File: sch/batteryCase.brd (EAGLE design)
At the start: 68.2 x 27.9 mm, 7 parts, among them X1 C-GRID-04-70553

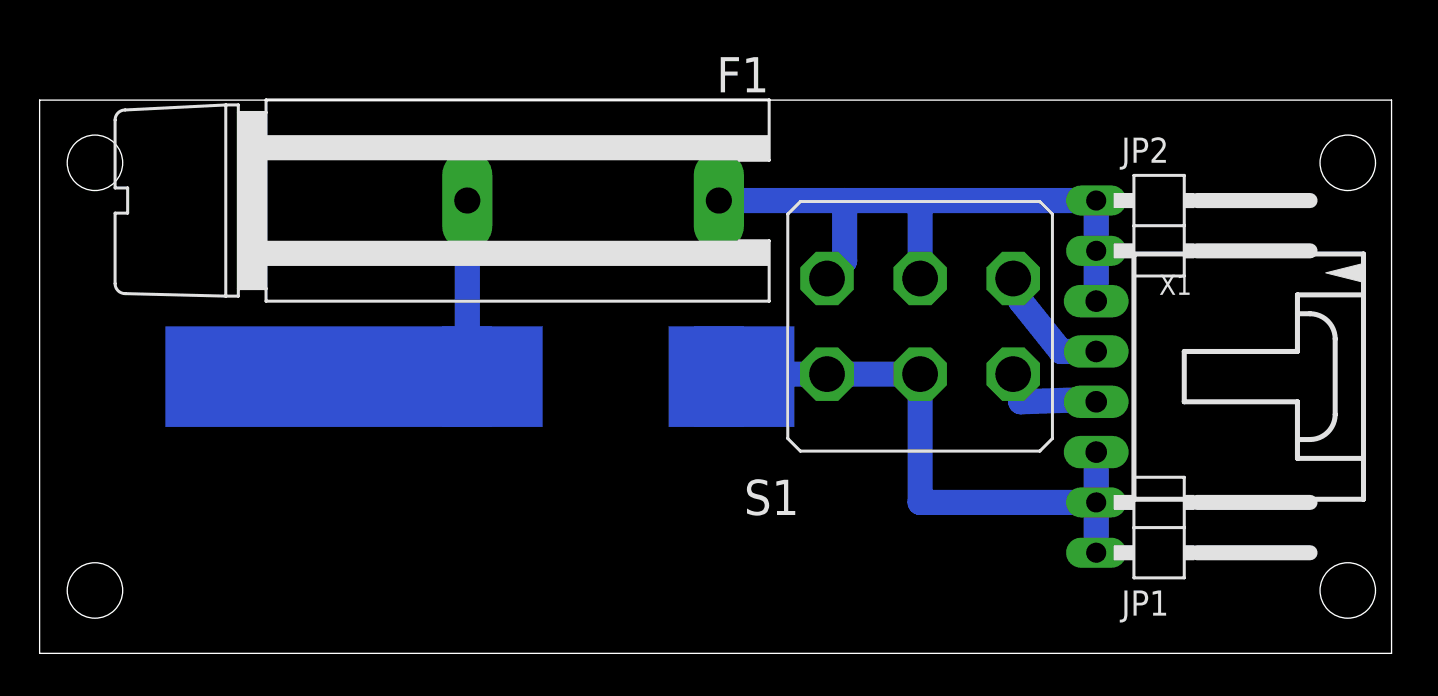
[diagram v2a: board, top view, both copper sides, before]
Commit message: Some copper plane for mechanical strength (and reminder about metal casing)
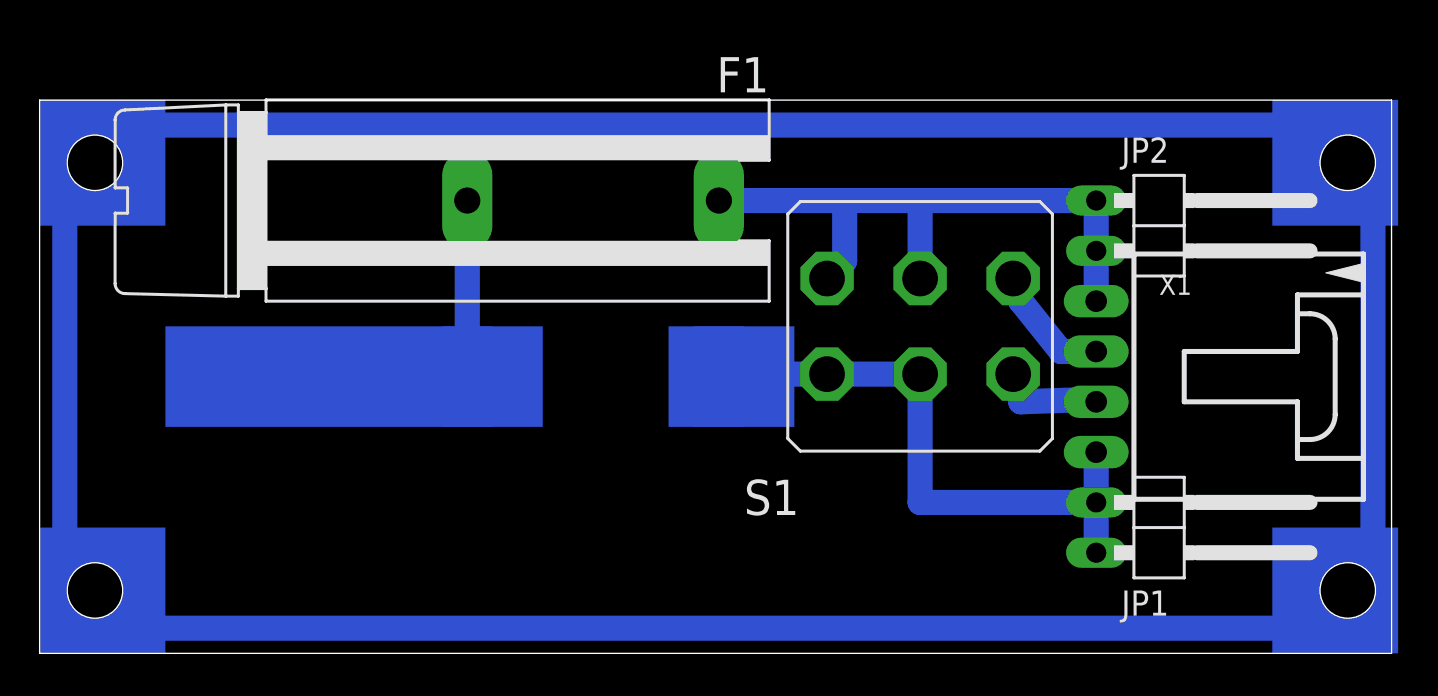
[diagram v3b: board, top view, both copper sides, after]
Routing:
- net N$6: track 0.00 -> 182.9 mm
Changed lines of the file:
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@@
 <hole x="66.04" y="3.175" drill="2.8"/>
 <hole x="66.04" y="24.765" drill="2.8"/>
+<rectangle x1="0" y1="0" x2="6.35" y2="6.35" layer="16"/>
+<rectangle x1="0" y1="21.59" x2="6.35" y2="27.94" layer="16"/>
+<rectangle x1="62.23" y1="21.59" x2="68.58" y2="27.94" layer="16"/>
+<rectangle x1="62.23" y1="0" x2="68.58" y2="6.35" layer="16"/>
 </plain>
 <attributes>
@@
 <wire x1="21.59" y1="22.86" x2="21.59" y2="13.97" width="1.27" layer="16"/>
 </signal>
+<signal name="N$6">
+<wire x1="1.27" y1="26.67" x2="67.31" y2="26.67" width="1.27" layer="16"/>
+<wire x1="67.31" y1="26.67" x2="67.31" y2="1.27" width="1.27" layer="16"/>
+<wire x1="67.31" y1="1.27" x2="1.27" y2="1.27" width="1.27" layer="16"/>
+<wire x1="1.27" y1="1.27" x2="1.27" y2="26.67" width="1.27" layer="16"/>
+</signal>
 </signals>
